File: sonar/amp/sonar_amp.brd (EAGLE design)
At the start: 101.3 x 81.3 mm, 40 parts, among them IC2 LMV797, IC3 LMV797, IC4 LMV797, IC5 LMV797, IC6 ADR510

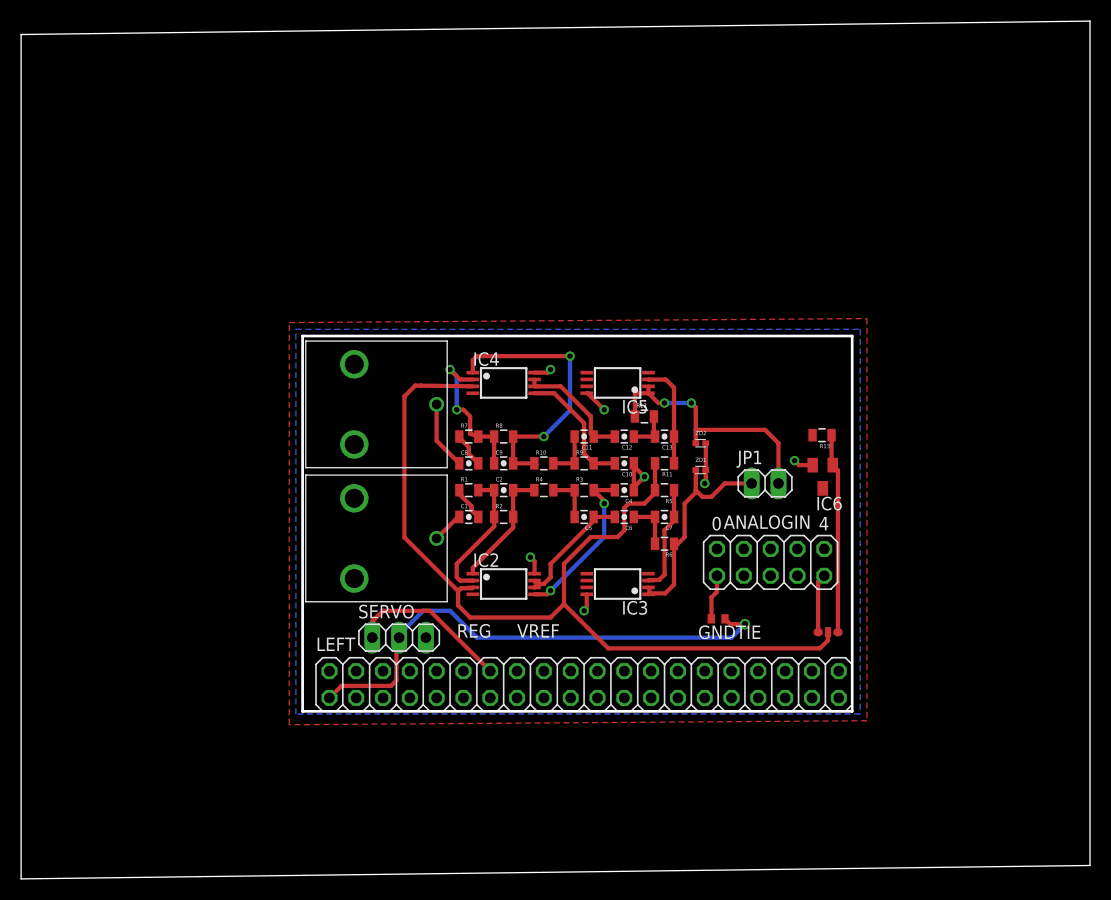
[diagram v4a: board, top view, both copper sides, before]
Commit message: Added extra PWM header
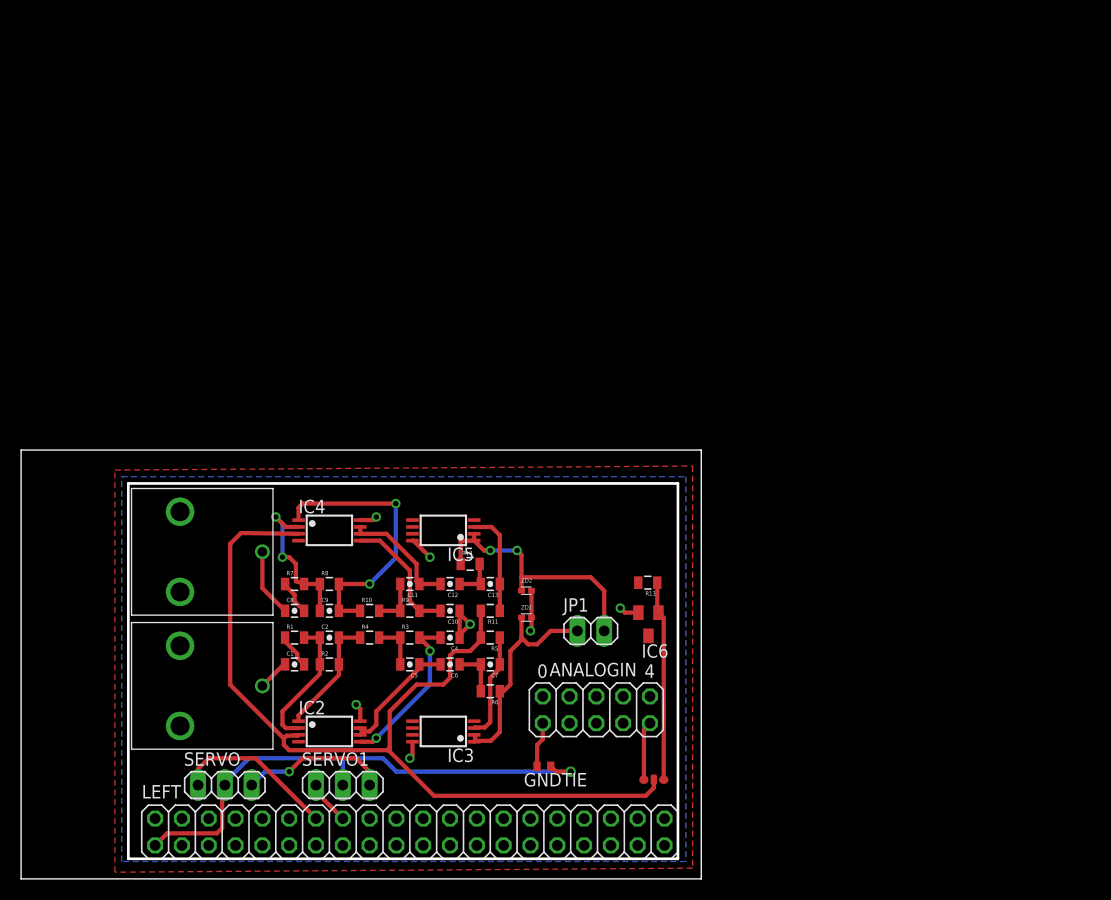
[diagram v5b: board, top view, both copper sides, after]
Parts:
- added SERVO1: (no value), pinhead:1X03
- IC2: value LMV797 -> (none)
- moved C10 21.6 mm to (39.4, 24.1)
- moved C4 21.6 mm to (39.4, 21.6)
- moved C6 21.6 mm to (39.4, 19.1)
- moved ANALOGIN 21.6 mm to (53.2, 14.8)
- moved C12 21.6 mm to (39.4, 26.7)
- moved IC6 21.6 mm to (58.2, 22.9)
- moved JP1 21.6 mm to (52.7, 22.2)
- moved C1 21.6 mm to (24.6, 19.1)
- moved C2 21.6 mm to (27.9, 21.6)
- moved C8 21.6 mm to (24.6, 24.1)
- moved C9 21.6 mm to (27.9, 24.1)
- moved IC2 21.6 mm to (27.9, 12.7)
- moved IC4 21.6 mm to (27.9, 31.8)
- moved R1 21.6 mm to (24.6, 21.6)
- moved R2 21.6 mm to (27.9, 19.1)
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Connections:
- net DGND: now also SERVO1.2
- net EHRPWM1B: now also SERVO1.1
- net VCC: now also SERVO1.3
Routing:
- net VCC: track 0.00 -> 14.0 mm, vias 0 -> 1
- net EHRPWM1B: track 0.00 -> 4.23 mm
- net DGND: track 48.8 -> 50.3 mm
- net 1V: track 88.5 -> 87.0 mm
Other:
- board size 101.3 x 81.3 mm -> 64.4 x 40.6 mm
- board text added: "PWM"
- board text removed: "REG"

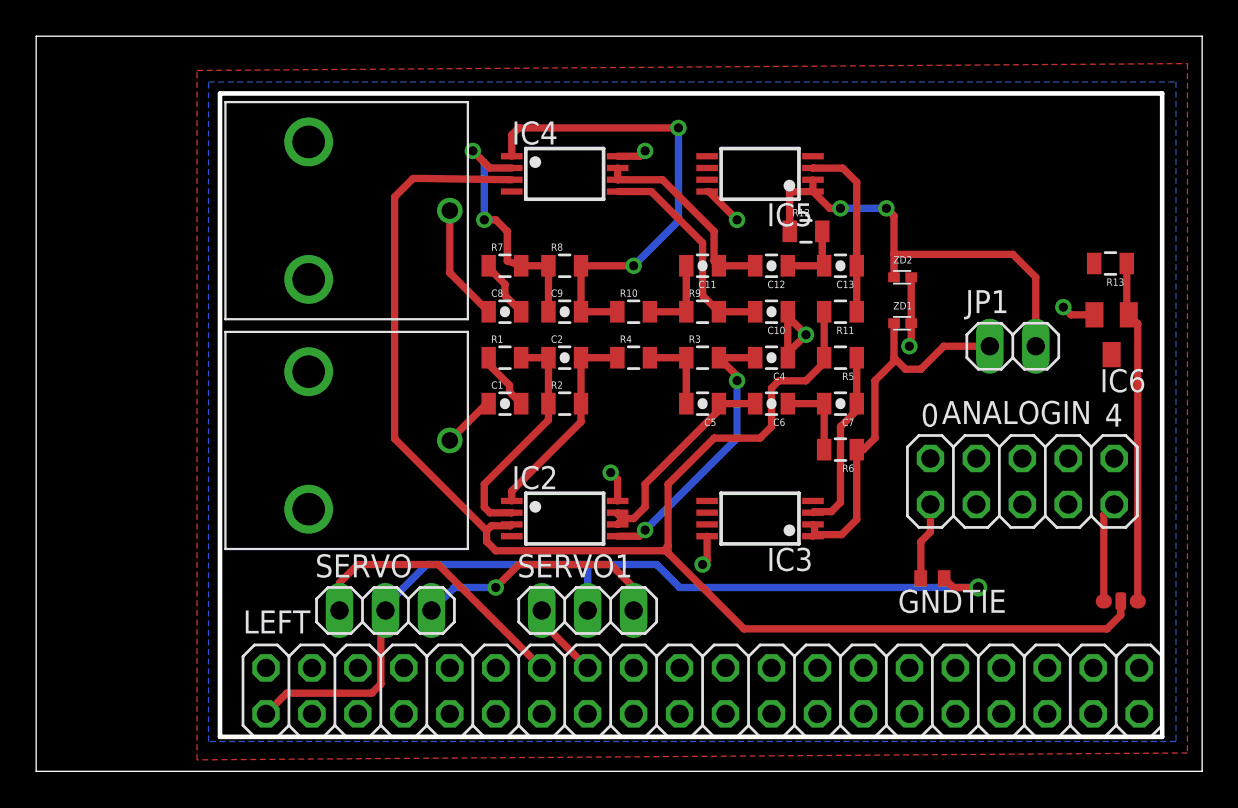
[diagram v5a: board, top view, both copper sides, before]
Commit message: Made aesthetic changes
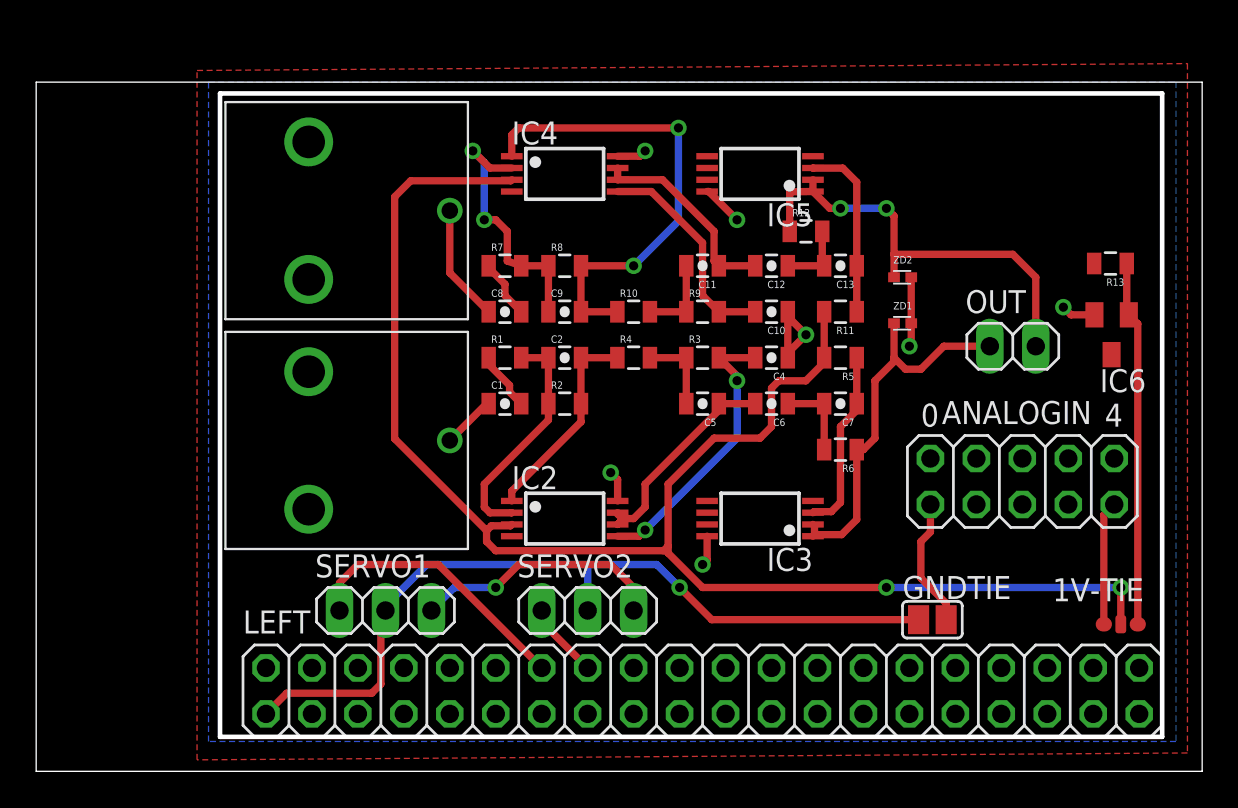
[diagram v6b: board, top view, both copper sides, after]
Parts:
- removed SERVO: (no value), pinhead:1X03
- added SERVO2: (no value), pinhead:1X03
- GNDTIE: device eagle-ltspice:R0402 -> jumper:SJ
- IC6: value ADR510 -> (none)
- moved SERVO1 11.2 mm to (18.0, 7.62)
- moved GNDTIE 2.29 mm to (48.3, 7.11)
- moved 1V-TIE 1.27 mm to (58.7, 6.86)
- renumbered JP1 to OUT
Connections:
- net AGND: now also GNDTIE.2; no longer GNDTIE.1
- net DGND: now also GNDTIE.1, SERVO2.2; no longer GNDTIE.2, SERVO.2
- net EHRPWM1A: now also SERVO1.1; no longer SERVO.1
- net EHRPWM1B: now also SERVO2.1; no longer SERVO1.1
- net VCC: now also SERVO2.3; no longer SERVO.3
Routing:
- net DGND: track 50.3 -> 45.7 mm
- net AGND: track 23.3 -> 26.2 mm
- net VREF: track 5.74 -> 7.01 mm
- net INDEP_1V: track 18.9 -> 20.2 mm
- net 1V: vias 0 -> 2
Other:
- board size 64.4 x 40.6 mm -> 64.4 x 38.1 mm
- board text added: "1"
- board text added: "2"
- board text removed: "VREF"

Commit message: Made LMV797 GND/VCC fix (good catch Brayden). A few more aesthetic adjustments
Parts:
- renumbered LEFT to P9
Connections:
- net AGND: now also IC2.4, IC3.4, IC4.4, IC5.4; no longer IC2.8, IC3.8, IC4.8, IC5.8
- net VCC: now also IC2.8, IC3.8, IC4.8, IC5.8; no longer IC2.4, IC3.4, IC4.4, IC5.4
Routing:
- net VCC: track 14.0 -> 5.35 mm
- net 1V: track 87.0 -> 95.3 mm
- net AGND: track 26.2 -> 25.2 mm

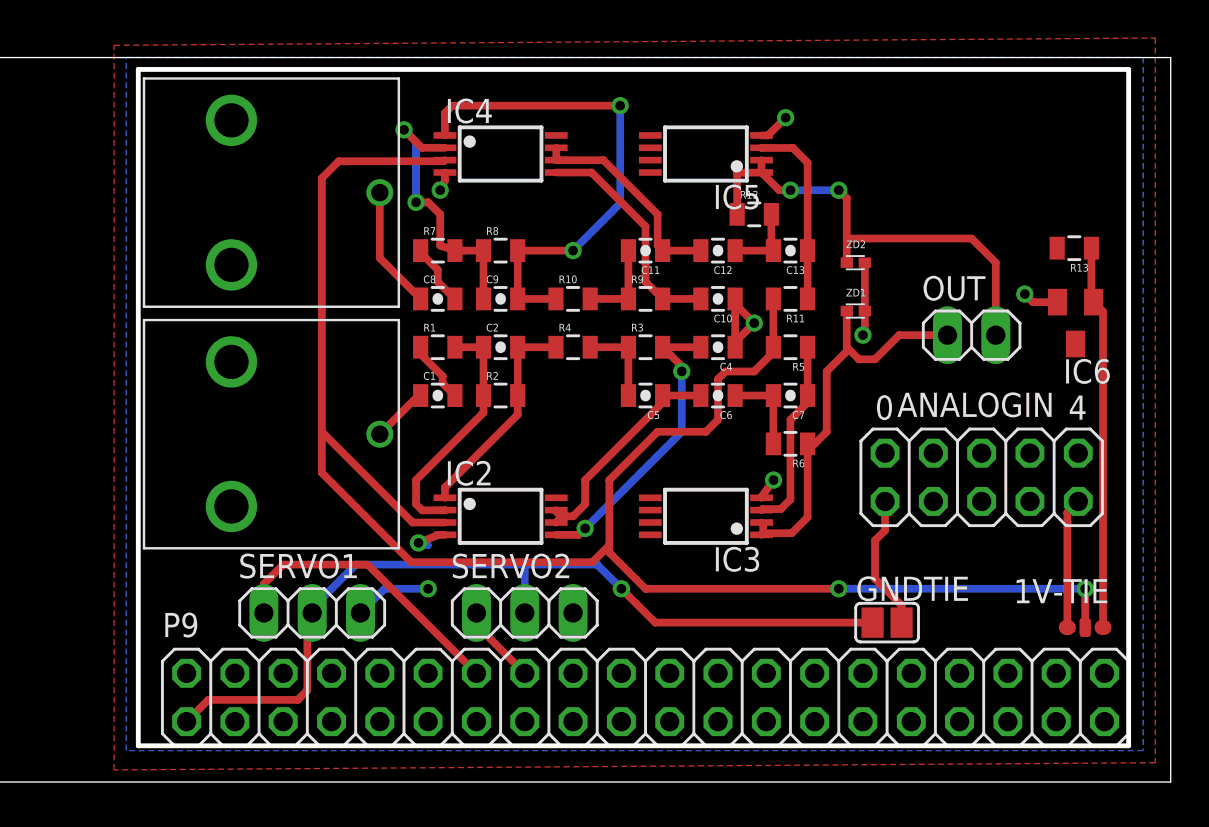
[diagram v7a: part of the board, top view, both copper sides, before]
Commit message: Added digital pots to I2C line. Moved servo lines. Servo 2 now overlays on top of PRUDAQ SMA header so we will need to desolder SMA header probably if we need to use  servo 2
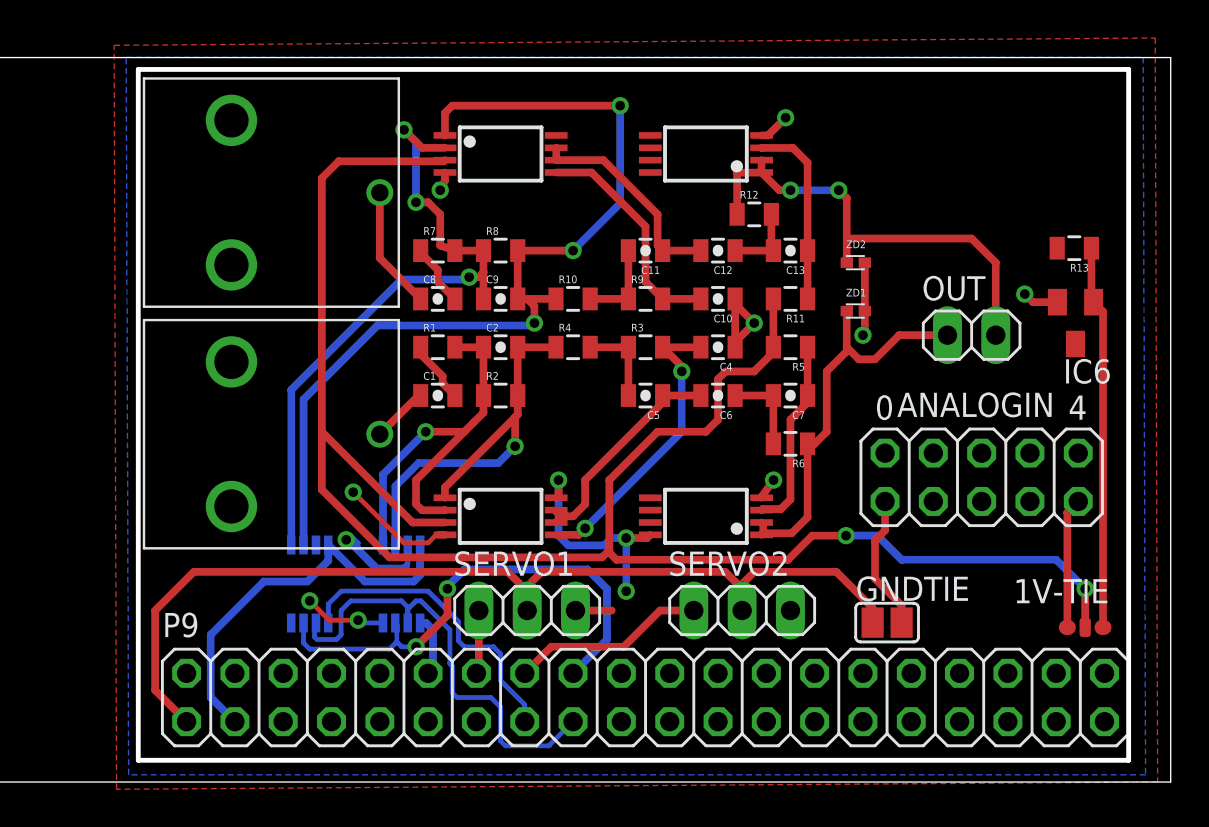
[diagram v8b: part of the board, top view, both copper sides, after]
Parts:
- added U$5, U$9: MCP4561, SONAR:MSOP8
- moved SERVO2 11.4 mm to (40.6, 7.75)
- moved SERVO1 11.3 mm to (29.3, 7.75)
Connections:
- removed net GPIO4: P9.17
- removed net GPIO_5: P9.18
- removed net N$102: C2.2, IC2.1, R2.2, R4.1
- removed net N$202: C9.2, IC4.1, R10.1, R8.2
- removed net POW: C2.1, IC2.2, R1.2, R2.1
- removed net POW1: C9.1, IC4.2, R7.2, R8.1
- new net I2C1_SCA: P9.18, U$5.3, U$9.3
- new net I2C1_SCL: P9.17, U$5.2, U$9.2
- new net P0A1: C2.1, IC2.2, R1.2, R2.1, U$5.5
- new net P0A2: C9.1, IC4.2, R7.2, R8.1, U$9.5
- new net P0W1: C2.2, IC2.1, R2.2, R4.1, U$5.6
- new net P0W2: C9.2, IC4.1, R10.1, R8.2, U$9.6
- net AGND: now also U$5.4, U$5.7, U$9.4, U$9.7
- net GPIO_48: now also U$9.1
- net GPIO_60: now also U$5.1
- net VDD_3V3: now also U$5.8, U$9.8
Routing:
- net P0W2: track 0.00 -> 49.5 mm, vias 0 -> 3
- net P0A2: track 0.00 -> 35.5 mm, vias 0 -> 3
- net N$202: track 26.7 -> 0.00 mm, vias 2 -> 0
- net I2C1_SCA: track 0.00 -> 26.6 mm, vias 0 -> 2
- net I2C1_SCL: track 0.00 -> 24.5 mm
- net P0W1: track 0.00 -> 23.3 mm, vias 0 -> 1
- net P0A1: track 0.00 -> 21.8 mm, vias 0 -> 1
- net VDD_3V3: track 0.00 -> 21.1 mm
- net AGND: track 25.2 -> 43.9 mm, vias 7 -> 10
- net GPIO_48: track 0.00 -> 16.4 mm
- net POW1: track 14.7 -> 0.00 mm, vias 2 -> 0
- net POW: track 12.9 -> 0.00 mm
- net EHRPWM1A: track 15.5 -> 3.35 mm
- net N$102: track 11.5 -> 0.00 mm
- net VCC: track 5.35 -> 13.9 mm, vias 1 -> 3
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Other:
- outline, holes or cut-outs redrawn
